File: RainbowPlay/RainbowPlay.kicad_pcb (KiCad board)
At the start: 2 copper layers, 80 x 60 mm, 11 parts, among them J1 GPIO_CONNECTOR

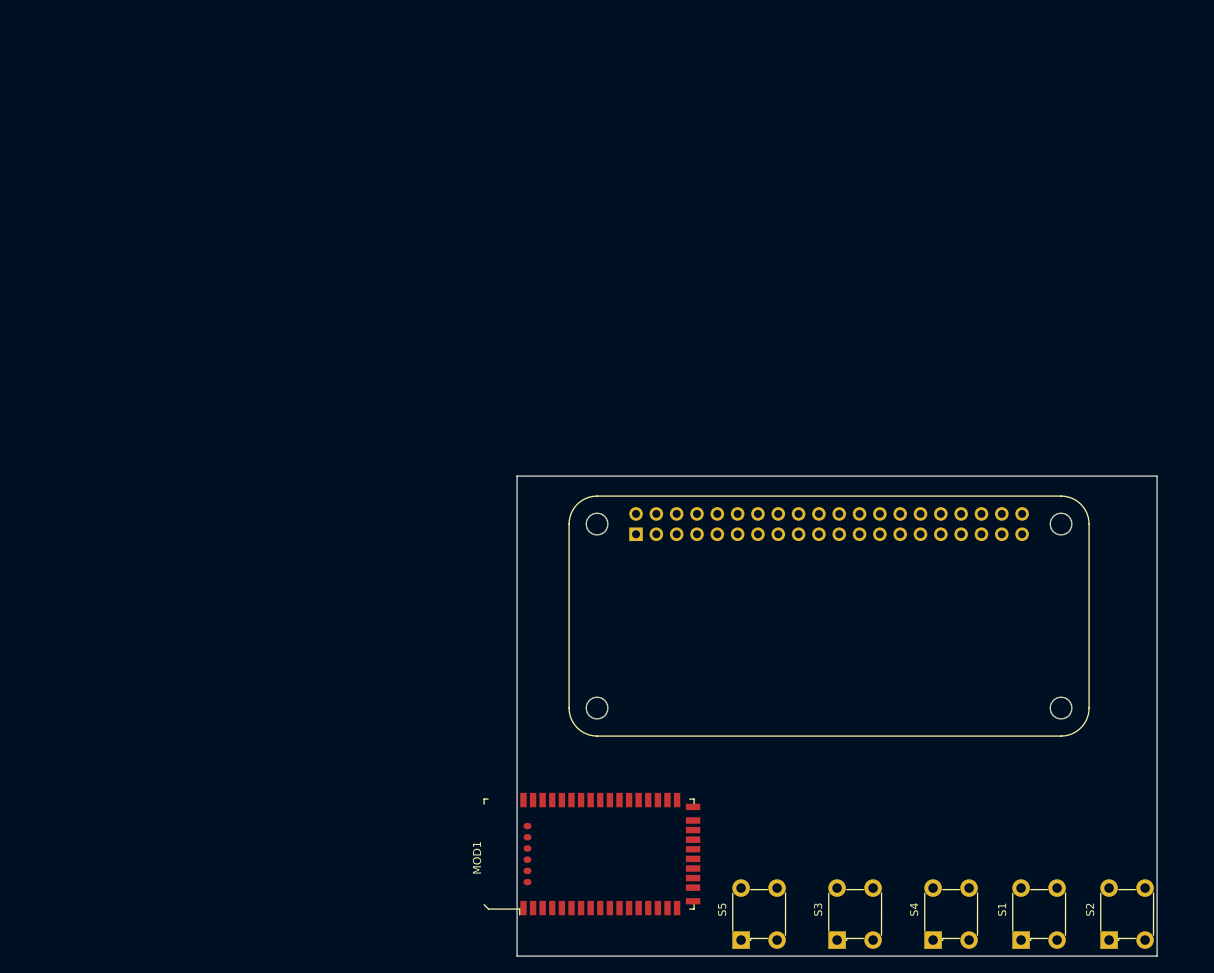
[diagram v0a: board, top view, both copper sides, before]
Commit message: General dev on PCB
Ensure GPIO pinouts are correct
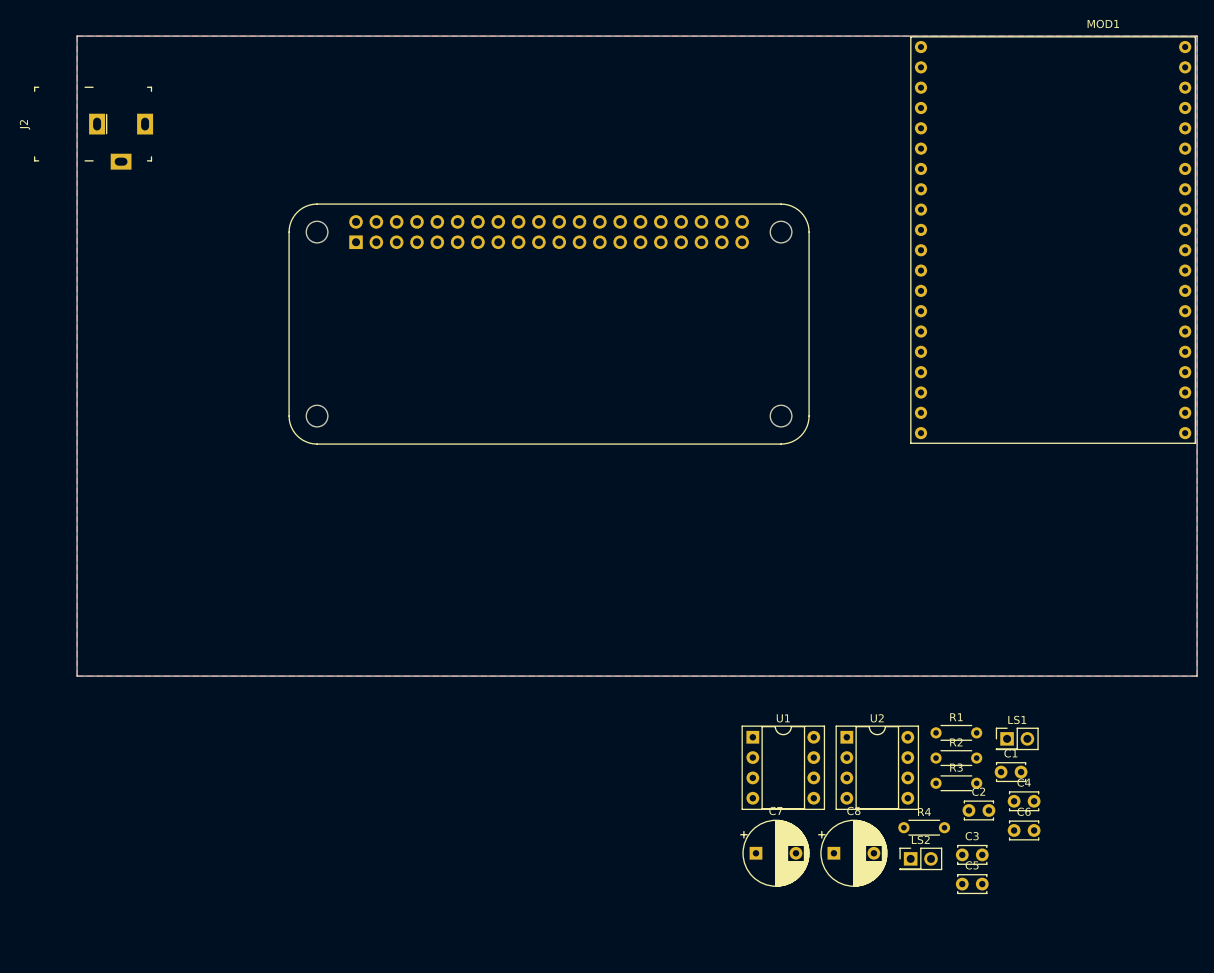
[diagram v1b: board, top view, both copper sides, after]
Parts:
- removed S1, S2, S3, S4, S5: 1825910-6, digikey-footprints:Switch_Tactile_THT_6x6mm
- added C1: 10uF, Capacitor_THT:C_Disc_D3.4mm_W2.1mm_P2.50mm, F.Cu at (171.5, 121.6)
- added C2: 10uF, Capacitor_THT:C_Disc_D3.4mm_W2.1mm_P2.50mm, F.Cu at (167.5, 126.4)
- added C3: 0.1uF, Capacitor_THT:C_Disc_D3.4mm_W2.1mm_P2.50mm, F.Cu at (166.7, 131.9)
- added C4: 0.1uF, Capacitor_THT:C_Disc_D3.4mm_W2.1mm_P2.50mm, F.Cu at (173.2, 125.2)
- added C5: 0.05uF, Capacitor_THT:C_Disc_D3.4mm_W2.1mm_P2.50mm, F.Cu at (166.7, 135.6)
- added C6: 0.05uF, Capacitor_THT:C_Disc_D3.4mm_W2.1mm_P2.50mm, F.Cu at (173.2, 128.9)
- added C7: 250uF, Capacitor_THT:CP_Radial_D8.0mm_P5.00mm, F.Cu at (140.9, 131.7)
- added C8: 250uF, Capacitor_THT:CP_Radial_D8.0mm_P5.00mm, F.Cu at (150.6, 131.7)
- added J2: PJ-102A, digikey-footprints:Barrel_Jack_5.5mmODx2.1mmID_PJ-102A, F.Cu at (61.5, 40.6)
- added LS1: Speaker, Connector_PinHeader_2.54mm:PinHeader_2x01_P2.54mm_Vertical, F.Cu at (172.3, 117.4)
- added LS2: Speaker, Connector_PinHeader_2.54mm:PinHeader_2x01_P2.54mm_Vertical, F.Cu at (160.2, 132.4)
- added R1: 1.2k, Resistor_THT:R_Axial_DIN0204_L3.6mm_D1.6mm_P5.08mm_Horizontal, F.Cu at (163.4, 116.7)
- added R2: 1.2k, Resistor_THT:R_Axial_DIN0204_L3.6mm_D1.6mm_P5.08mm_Horizontal, F.Cu at (163.4, 119.8)
- added R3: 10R, Resistor_THT:R_Axial_DIN0204_L3.6mm_D1.6mm_P5.08mm_Horizontal, F.Cu at (163.4, 123.0)
- added R4: 10R, Resistor_THT:R_Axial_DIN0204_L3.6mm_D1.6mm_P5.08mm_Horizontal, F.Cu at (159.4, 128.5)
- added U1: LM386, Package_DIP:DIP-8_W7.62mm_Socket, F.Cu at (140.5, 117.2)
- added U2: LM386, Package_DIP:DIP-8_W7.62mm_Socket, F.Cu at (152.3, 117.2)
- MOD1: footprint digikey-footprints:Bluetooth_Module_RN52-IRM -> kicad-footprints:rn52-breakout
- moved MOD1 94.9 mm to (178.0, 55.1), turned to 0 degrees
- moved H1 50.6 mm to (86.0, 54.1)
- moved H2 50.6 mm to (144.0, 54.1)
- moved H3 50.6 mm to (144.0, 77.1)
- moved H4 50.6 mm to (86.0, 77.1)
- moved J1 50.6 mm to (90.9, 55.3)
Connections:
- net +5V renamed +15V
- J1 pad 14: GND -> (no net)
- J1 pad 20: GND -> (no net)
- J1 pad 25: GND -> (no net)
- J1 pad 30: GND -> (no net)
- J1 pad 34: GND -> (no net)
- J1 pad 6: GND -> (no net)
- J1 pad 9: GND -> (no net)
- MOD1 pad 10: /VOL_DWN -> (no net)
- MOD1 pad 21: (no net) -> +3V3
- MOD1 pad 40: (no net) -> /SPK_R-
- MOD1 pad 41: (no net) -> /SPK_L-
- MOD1 pad 42: (no net) -> /SPK_R+
- MOD1 pad 43: (no net) -> /SPK_L+
- MOD1 pad 6: /VOL_UP -> (no net)
- MOD1 pad 7: /NXT_TRK -> (no net)
- MOD1 pad 8: /PLY_PS -> (no net)
- MOD1 pad 9: /PREV_TRK -> (no net)
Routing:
- added copper zone on F.Cu, net GND
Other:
- board size 80 x 60 mm -> 140 x 80 mm
